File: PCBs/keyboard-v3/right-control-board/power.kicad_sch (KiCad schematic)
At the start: 10 parts, among them U701 TPS62290TDRVRQ1

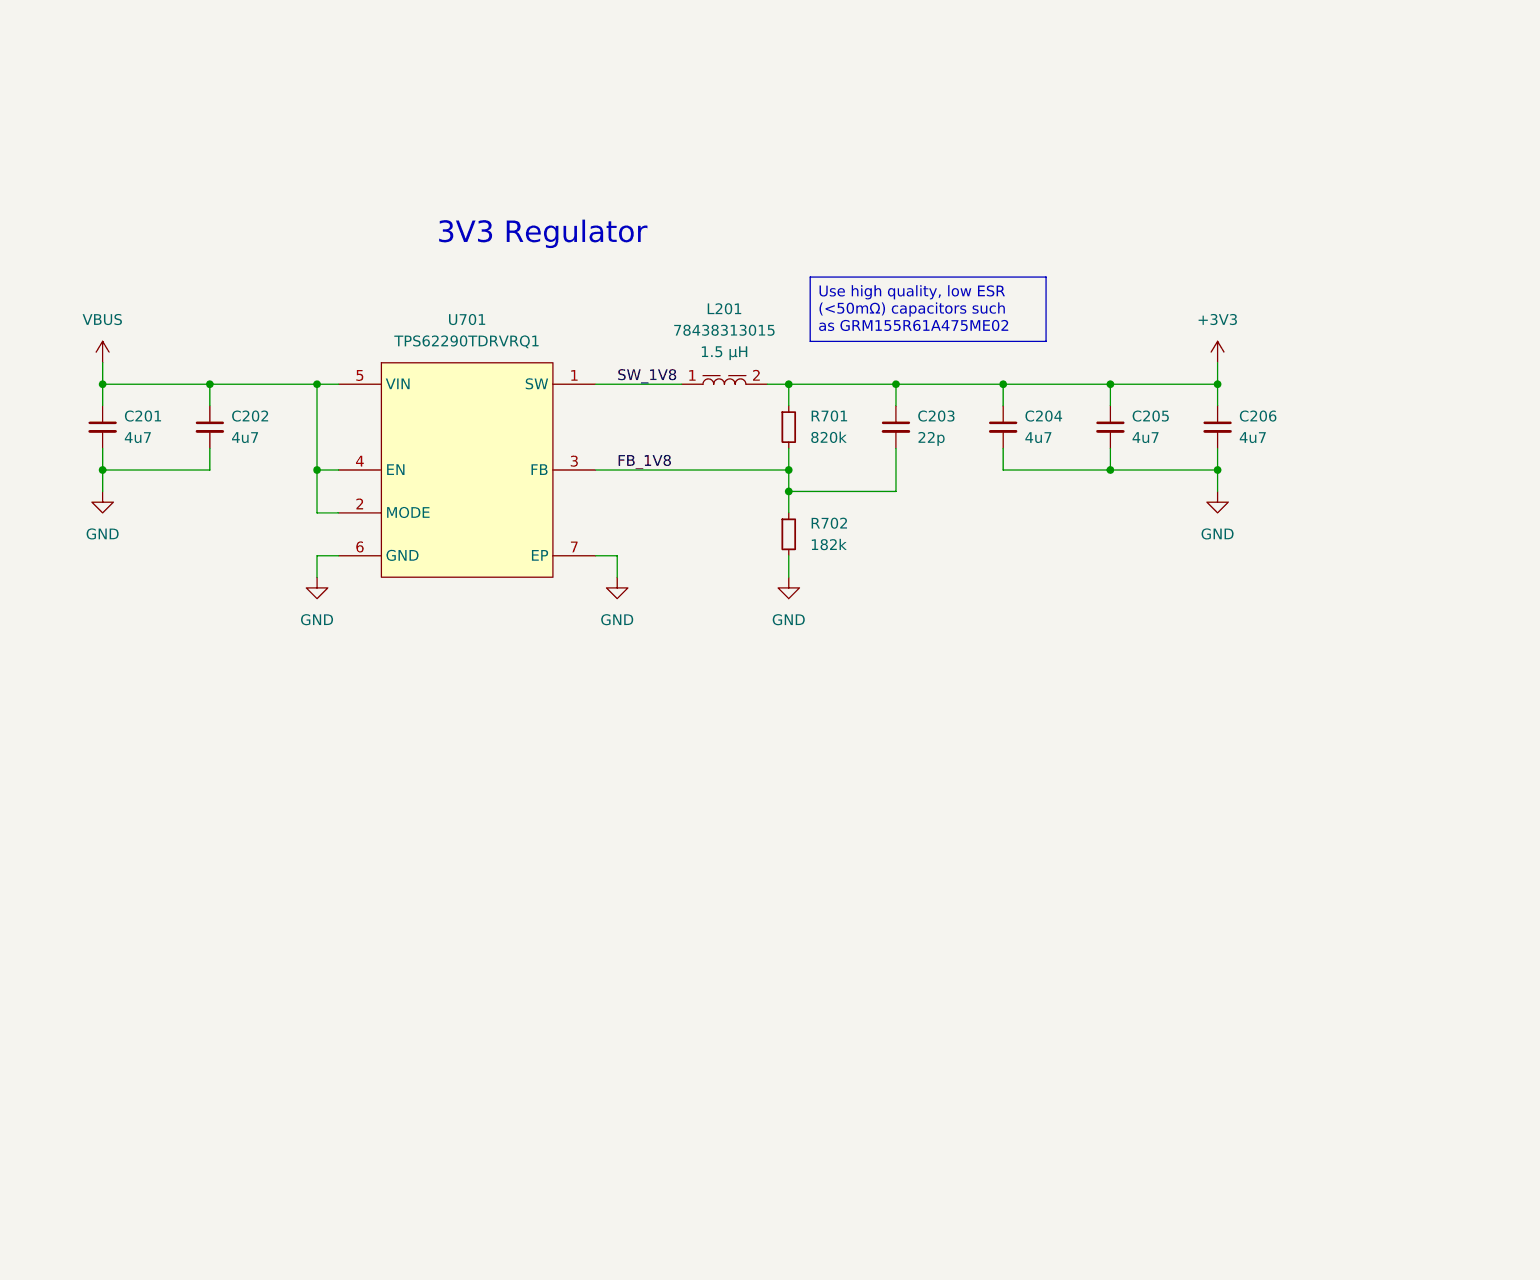
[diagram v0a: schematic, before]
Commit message: Added debug-breakout board, progress on right side schematics & layout
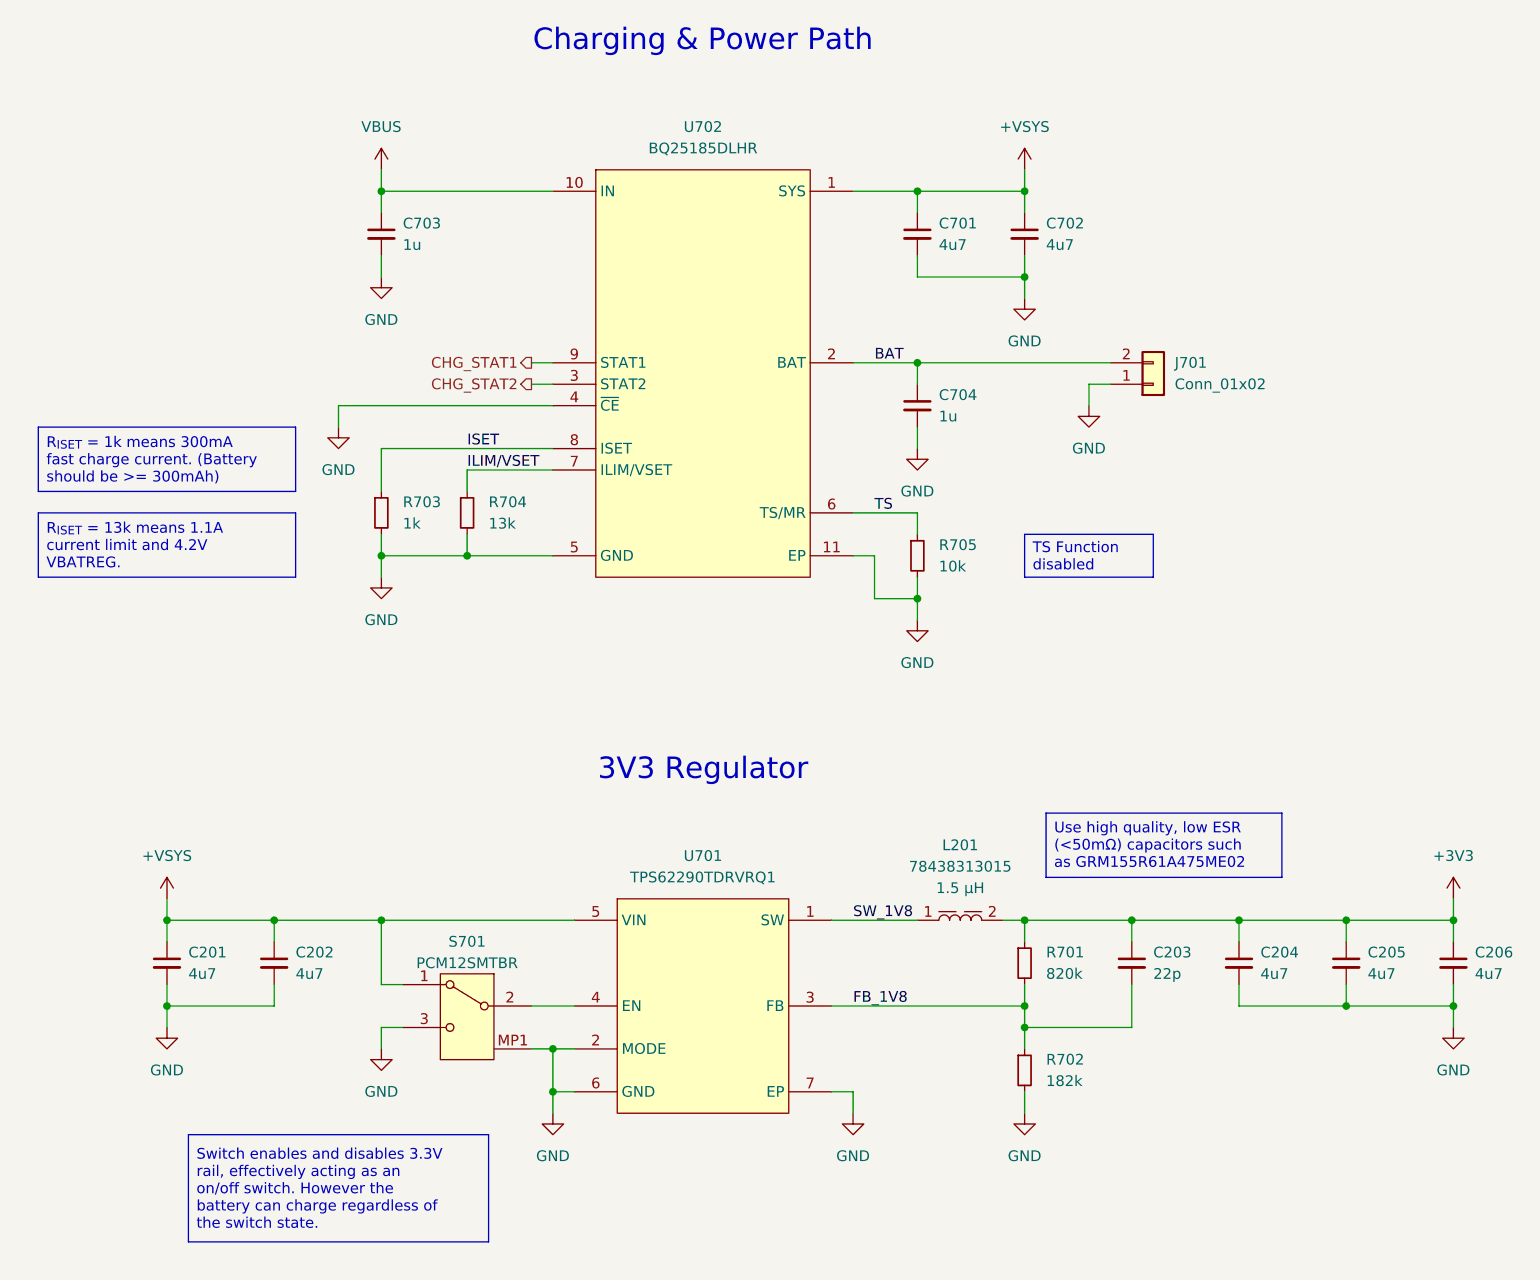
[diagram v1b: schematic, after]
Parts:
- added C701, C702: 4u7, project_footprints:C_0402, symbol DEV:C_SMALL
- added C703, C704: 1u, project_footprints:C_0402, symbol DEV:C_SMALL
- added J701: Conn_01x02, Connector_JST:JST_PH_S2B-PH-K_1x02_P2.00mm_Horizontal, symbol Connector_Generic:Conn_01x02
- added R703: 1k, project_footprints:R_0402, symbol DEV:R_SMALL
- added R704: 13k, project_footprints:R_0402, symbol DEV:R_SMALL
- added R705: 10k, project_footprints:R_0402, symbol DEV:R_SMALL
- added S701: PCM12SMTBR, project_footprints:PCM12SMTBR, symbol MECH:PCM12SMTBR
- added U702: BQ25185DLHR, project_footprints:SON40P220X200X80-11N, symbol CHARGING:BQ25185DLHR
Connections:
- net GND: now also U701.2 (MODE), C701.2, C702.2, C703.2, C704.2, J701.1 (Pin_1), R703.2, R704.2, R705.2, S701.3 (NO), S701.MP1, S701.MP2, S701.MP3, S701.MP4, U702.11 (EP), U702.4 (~{CE}), U702.5 (GND)
- net VBUS: now also C703.1, U702.10 (IN); no longer C201.1, C202.1, U701.2 (MODE), U701.4 (EN), U701.5 (VIN)
- new net: S701.2 (COM), U701.4 (EN)
- new net +VSYS: C201.1, C202.1, C701.1, C702.1, S701.1 (NC), U701.5 (VIN), U702.1 (SYS)
- new net BAT: C704.1, J701.2 (Pin_2), U702.2 (BAT)
- new net CHG_STAT1: U702.9 (STAT1)
- new net CHG_STAT2: U702.3 (STAT2)
- new net ILIM/VSET: R704.1, U702.7 (ILIM/VSET)
- new net ISET: R703.1, U702.8 (ISET)
- new net TS: R705.1, U702.6 (TS/MR)
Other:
- note added: "Charging & Power Path"
- moved on the sheet: C201, C202, C203, C204, C205, C206, L201, R701, R702, U701

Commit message: Right control board placement and schematic done
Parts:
- added D701: RED, project_footprints:LED_0402, symbol Device:D_Small
- added R706: 10k, project_footprints:R_0402, symbol DEV:R_SMALL
- R701: value 820k -> 806k
- R702: value 182k -> 180k
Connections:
- net VBUS: now also R706.1
- net EN: now reaches S701.2 (COM), U701.4 (EN)
- net CHG_STAT1 renamed STAT1
- net STAT1: now also D701.2 (A), R706.2
- net CHG_STAT2 renamed STAT2
- net STAT2: now also D701.1 (K)
- net FB_1V8 renamed FB_3V3
- net SW_1V8 renamed SW_3V3
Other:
- moved on the sheet: C201, C202, C203, C204, C205, C206, C701, C702, C703, C704, J701, L201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

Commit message: Added mounting holes
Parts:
- renumbered C703 to C701, C701 to C702, C702 to C703, C201 to C705, C202 to C706, C203 to C707, C204 to C708, C205 to C709, C206 to C710, L201 to L701, R706 to R701, R703 to R702, R704 to R703, R705 to R704, R701 to R705, R702 to R706, U702 to U701, U701 to U702

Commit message: Added v3 left BOMs and updated buck inductor
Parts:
- L701: value 78438313015 -> 74438313015; footprint project_footprints:L_Wurth_WE-MAIA-1610 -> project_footprints:L_Wurth_WE-MAPI-1610; symbol PWR-IND:1610_78438313015 -> PWR-IND:74438313015; Match Code WE-MAIA -> WE-MAPI; Part Number 78438313015 -> 74438313015; Published Date 20250429 -> 20250320; RDC typ. (mΩ) (none) -> 189.0; VOP (V) (none) -> 80
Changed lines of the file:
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@@
 	)
 	(symbol
-		(lib_id "PWR-IND:1610_78438313015")
+		(lib_id "PWR-IND:74438313015")
 		(at 182.88 129.54 0)
 		(unit 1)
@@
 			)
 		)
-		(property "Value" "78438313015"
+		(property "Value" "74438313015"
 			(at 182.88 123.19 0)
 			(effects
@@
 			)
 		)
-		(property "Footprint" "project_footprints:L_Wurth_WE-MAIA-1610"
-			(at 195.58 109.22 0)
+		(property "Footprint" "project_footprints:L_Wurth_WE-MAPI-1610"
+			(at 182.88 121.92 0)
 			(effects
 				(font
 					(size 1.27 1.27)
 				)
-				(justify left)
 				(hide yes)
 			)
 		)
-		(property "Datasheet" "https://www.we-online.com/catalog/datasheet/78438313015.pdf?ki"
-			(at 195.58 111.76 0)
+		(property "Datasheet" "https://www.we-online.com/catalog/datasheet/74438313015.pdf?ki"
+			(at 234.95 111.76 0)
 			(effects
 				(font
 					(size 1.27 1.27)
 				)
-				(justify left)
 				(hide yes)
 			)
 		)
-		(property "Description" "Single Coil Power Inductor"
+		(property "Description" "Shielded Power Inductor"
 			(at 182.88 129.54 0)
 			(effects
@@
 		)
 		(property "Manufacturer" "Wurth Elektronik"
-			(at 195.58 114.3 0)
+			(at 234.95 114.3 0)
 			(effects
 				(font
 					(size 1.27 1.27)
 				)
-				(justify left)
 				(hide yes)
 			)
 		)
 		(property "Manufacturer URL" "https://www.we-online.com"
-			(at 195.58 116.84 0)
+			(at 234.95 116.84 0)
 			(effects
 				(font
 					(size 1.27 1.27)
 				)
-				(justify left)
 				(hide yes)
 			)
 		)
-		(property "Published Date" "20250429"
-			(at 195.58 119.38 0)
+		(property "Published Date" "20250320"
+			(at 234.95 119.38 0)
 			(effects
 				(font
 					(size 1.27 1.27)
 				)
-				(justify left)
 				(hide yes)
 			)
 		)
-		(property "Match Code" "WE-MAIA"
-			(at 195.58 121.92 0)
+		(property "Match Code" "WE-MAPI"
+			(at 234.95 121.92 0)
 			(effects
 				(font
 					(size 1.27 1.27)
 				)
-				(justify left)
 				(hide yes)
 			)
 		)
-		(property "Part Number" "78438313015"
-			(at 195.58 124.46 0)
+		(property "Part Number" "74438313015"
+			(at 234.95 124.46 0)
 			(effects
 				(font
 					(size 1.27 1.27)
 				)
-				(justify left)
 				(hide yes)
 			)
 		)
 		(property "Size" "1610"
-			(at 195.58 127 0)
+			(at 234.95 127 0)
 			(effects
 				(font
 					(size 1.27 1.27)
 				)
-				(justify left)
 				(hide yes)
 			)
 		)
 		(property "Mounting Technology" "SMT"
-			(at 195.58 129.54 0)
+			(at 234.95 129.54 0)
 			(effects
 				(font
 					(size 1.27 1.27)
 				)
-				(justify left)
 				(hide yes)
 			)
 		)
 		(property "L (µH)" "1.5"
-			(at 195.58 132.08 0)
+			(at 234.95 132.08 0)
 			(effects
 				(font
 					(size 1.27 1.27)
 				)
-				(justify left)
 				(hide yes)
 			)
@@
 		)
 		(property "ISAT,30% (A)" "3.45"
-			(at 195.58 137.16 0)
+			(at 234.95 137.16 0)
 			(effects
 				(font
 					(size 1.27 1.27)
 				)
-				(justify left)
 				(hide yes)
 			)
@@
 		)
 		(property "fres (MHz)" "90.0"
-			(at 195.58 142.24 0)
+			(at 234.95 142.24 0)
 			(effects
 				(font
 					(size 1.27 1.27)
 				)
-				(justify left)
 				(hide yes)
 			)
 		)
 		(property "IRP,40K (A)" "1.8"
-			(at 195.58 144.78 0)
+			(at 234.95 134.62 0)
 			(effects
 				(font
 					(size 1.27 1.27)
 				)
-				(justify left)
 				(hide yes)
 			)
@@
 			)
 		)
+		(property "RDC typ. (mΩ)" "189.0"
+			(at 234.95 139.7 0)
+			(effects
+				(font
+					(size 1.27 1.27)
+				)
+				(hide yes)
+			)
+		)
+		(property "VOP (V)" "80"
+			(at 234.95 144.78 0)
+			(effects
+				(font
+					(size 1.27 1.27)
+				)
+				(hide yes)
+			)
+		)
